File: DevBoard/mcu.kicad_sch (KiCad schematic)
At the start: 36 parts, among them J301 SWD, J302 UART debug, J303 Spare GPIO, U301 STM32WB1MMC

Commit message: Dev board: project footprints for holder, USB-C, half-bridge, module, EEPROM, BQ25756
- tools/make_footprints.py generates MonolithDev.pretty from the datasheets:
  BH-21700-B1BJ001 holder, Shou Han USB-C (with board-edge cutout),
  Infineon PG-TDSON-8-57 half-bridge (land + stencil), STM32WB1MMC LGA77,
  ST UFDFPN8 2x3 with the correct 1.2x1.4 exposed pad, and a 10 A net tie
- BQ25756 RRV0036A footprint from Antmicro (Apache-2.0), checked against TI
- Footprints assigned; R430/R530 become net-tie links, off the BOM and CPL
- Every symbol pin has a pad and vice versa; nets, ERC and overlaps unchanged

Co-Authored-By: Claude Opus 5.5 <noreply@anthropic.com>
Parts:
- U301: footprint (none) -> MonolithDev:ST_LGA-77_STM32WB1MMC_6.5x10mm
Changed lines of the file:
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@@
 		)
 		(property "Value" "0R"
-			(at 126.85 98.80 90)
+			(at 126.85 98.8 90)
 			(show_name no)
 			(do_not_autoplace no)
@@
 		(dnp no)
 		(property "Reference" "TH302"
-			(at 66.80 204.62 0)
+			(at 66.8 204.62 0)
 			(show_name no)
 			(do_not_autoplace no)
@@
 		)
 		(property "Value" "10k B3435"
-			(at 66.80 206.59 0)
+			(at 66.8 206.59 0)
 			(show_name no)
 			(do_not_autoplace no)
@@
 		(dnp no)
 		(property "Reference" "TH303"
-			(at 92.20 204.62 0)
+			(at 92.2 204.62 0)
 			(show_name no)
 			(do_not_autoplace no)
@@
 		)
 		(property "Value" "10k B3435"
-			(at 92.20 206.59 0)
+			(at 92.2 206.59 0)
 			(show_name no)
 			(do_not_autoplace no)
@@
 		(dnp no)
 		(property "Reference" "D301"
-			(at 71.43 237.80 0)
+			(at 71.43 237.8 0)
 			(show_name no)
 			(do_not_autoplace no)
@@
 		(dnp no)
 		(property "Reference" "TH304"
-			(at 117.60 204.62 0)
+			(at 117.6 204.62 0)
 			(show_name no)
 			(do_not_autoplace no)
@@
 		)
 		(property "Value" "10k B3435"
-			(at 117.60 206.59 0)
+			(at 117.6 206.59 0)
 			(show_name no)
 			(do_not_autoplace no)
@@
 		(dnp no)
 		(property "Reference" "U301"
-			(at 190.50 108.01 0)
+			(at 190.5 108.01 0)
 			(show_name no)
 			(do_not_autoplace no)
@@
 		)
 		(property "Value" "STM32WB1MMC"
-			(at 190.50 109.98 0)
+			(at 190.5 109.98 0)
 			(show_name no)
 			(do_not_autoplace no)
@@
 			)
 		)
-		(property "Footprint" ""
+		(property "Footprint" "MonolithDev:ST_LGA-77_STM32WB1MMC_6.5x10mm"
 			(at 190.5 139.7 0)
 			(hide yes)
@@
 		)
 		(property "Value" "GND"
-			(at 76.20 213.87 0)
+			(at 76.2 213.87 0)
 			(show_name no)
 			(do_not_autoplace no)
@@
 		(dnp no)
 		(property "Reference" "C311"
-			(at 139.87 200.80 0)
+			(at 139.87 200.8 0)
 			(show_name no)
 			(do_not_autoplace no)
@@
 		)
 		(property "Value" "GND"
-			(at 101.60 213.87 0)
+			(at 101.6 213.87 0)
 			(show_name no)
 			(do_not_autoplace no)
@@
 		)
 		(property "Value" "GND"
-			(at 161.22 127.00 90)
+			(at 161.22 127 90)
 			(show_name no)
 			(do_not_autoplace no)
@@
 		)
 		(property "Value" "GND"
-			(at 127.00 213.87 0)
+			(at 127 213.87 0)
 			(show_name no)
 			(do_not_autoplace no)
@@
 		(dnp no)
 		(property "Reference" "TH301"
-			(at 41.40 204.62 0)
+			(at 41.4 204.62 0)
 			(show_name no)
 			(do_not_autoplace no)
@@
 		)
 		(property "Value" "10k B3435"
-			(at 41.40 206.59 0)
+			(at 41.4 206.59 0)
 			(show_name no)
 			(do_not_autoplace no)
@@
 		)
 		(property "Value" "GND"
-			(at 50.80 213.87 0)
+			(at 50.8 213.87 0)
 			(show_name no)
 			(do_not_autoplace no)
@@
 		(dnp no)
 		(property "Reference" "J302"
-			(at 304.80 129.60 0)
+			(at 304.8 129.6 0)
 			(show_name no)
 			(do_not_autoplace no)
@@
 		)
 		(property "Value" "UART debug"
-			(at 304.80 131.57 0)
+			(at 304.8 131.57 0)
 			(show_name no)
 			(do_not_autoplace no)
@@
 		)
 		(property "Value" "GND"
-			(at 139.70 113.54 0)
+			(at 139.7 113.54 0)
 			(show_name no)
 			(do_not_autoplace no)
@@
 		(dnp no)
 		(property "Reference" "J303"
-			(at 312.90 164.12 0)
+			(at 312.9 164.12 0)
 			(show_name no)
 			(do_not_autoplace no)
@@
 		)
 		(property "Value" "Spare GPIO"
-			(at 312.90 166.08 0)
+			(at 312.9 166.08 0)
 			(show_name no)
 			(do_not_autoplace no)
@@
 		(dnp no)
 		(property "Reference" "TP305"
-			(at 292.10 258.31 0)
+			(at 292.1 258.31 0)
 			(show_name no)
 			(do_not_autoplace no)
@@
 		)
 		(property "Value" "GND"
-			(at 93.98 250.70 0)
+			(at 93.98 250.7 0)
 			(show_name no)
 			(do_not_autoplace no)

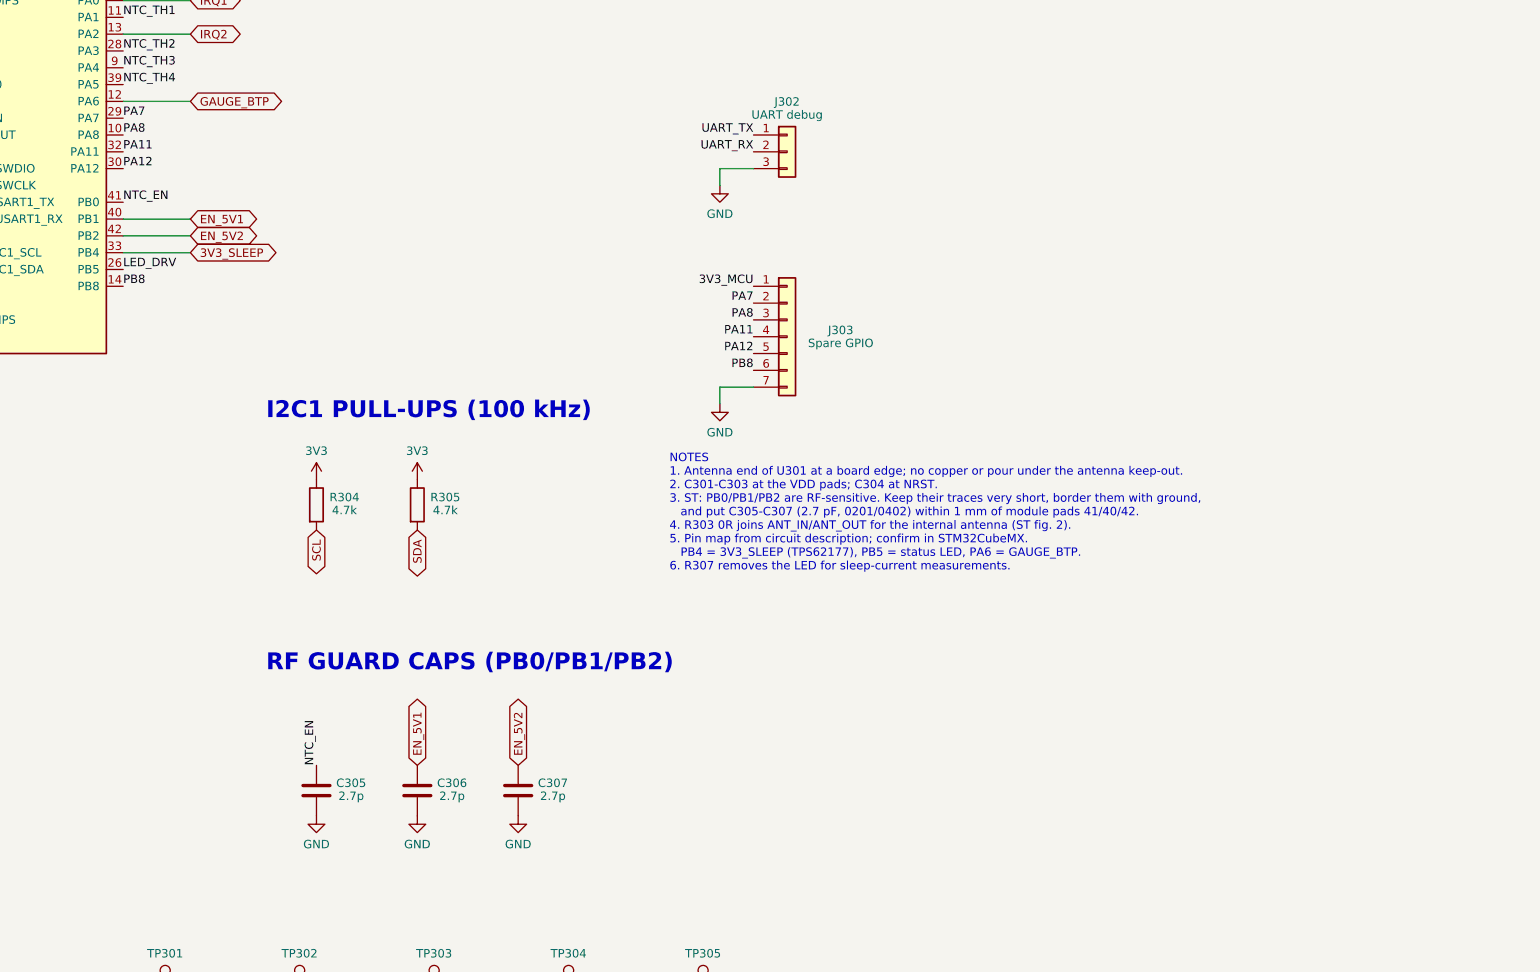
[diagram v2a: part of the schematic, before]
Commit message: Dev board design review: free PB0-PB2, document PB4 reset state
- NTC_EN, EN_5V1, EN_5V2 move from PB0/PB1/PB2 (ST: RF-sensitive, leave
  unconnected) to PA8/PA11/PA12; C305-C307 guard caps removed, no-connects added;
  J303 now brings out PA7, PB8 and the three enables
- Pin map checked against DS13258 table 15 (ADC, wake-up, I2C1, USART1, SWD)
- PB4 resets as NJTRST with pull-up, so the TPS62177 boots in normal mode,
  not sleep mode as documented; notes and docs corrected
- MCU notes: module placement per ST's reference PCB

Co-Authored-By: Claude Opus 5.5 <noreply@anthropic.com>
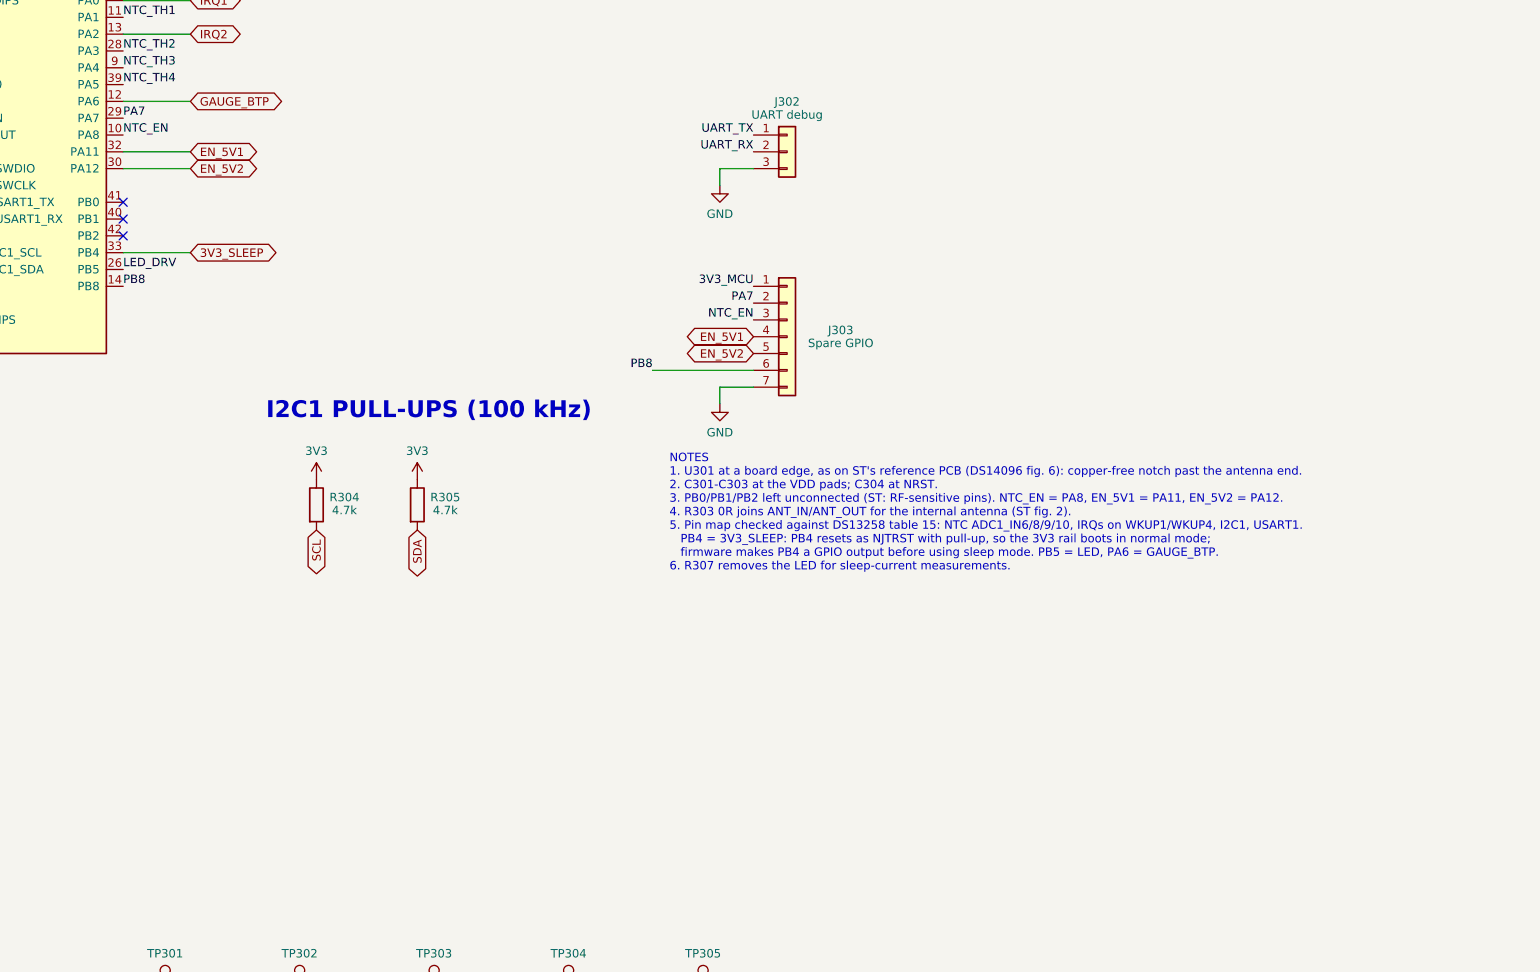
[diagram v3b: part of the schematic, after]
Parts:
- removed C305, C306, C307: 2.7p, Capacitor_SMD:C_0402_1005Metric, symbol Device:C
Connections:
- net PA11 is gone; now on net EN_5V1: J303.4 (Pin_4), U301.32 (PA11)
- net PA12 is gone; now on net EN_5V2: J303.5 (Pin_5), U301.30 (PA12)
- net PA8 is gone; now on net NTC_EN: J303.3 (Pin_3), U301.10 (PA8)
- net EN_5V1: no longer U301.40 (PB1)
- net EN_5V2: no longer U301.42 (PB2)
- net NTC_EN: no longer U301.41 (PB0)
- no-connect marks 3 -> 6
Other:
- note added: "NOTES 1. U301 at a board edge, as on ST's reference PCB (DS14096 fig. 6): copper-free notch past the antenna end. 2. C301-C303 at the VDD pads; C304 at NRST. 3. PB0/PB1/PB2 left unconnected (ST: RF-sensitive pins). NTC_EN = PA8, EN_5V1 = PA11, EN_5V2 = PA12. 4. R303 0R joins ANT_IN/ANT_OUT for the internal antenna (ST fig. 2). 5. Pin map checked against DS13258 table 15: NTC ADC1_IN6/8/9/10, IRQs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"
- note removed: "NOTES 1. Antenna end of U301 at a board edge; no copper or pour under the antenna keep-out. 2. C301-C303 at the VDD pads; C304 at NRST. 3. ST: PB0/PB1/PB2 are RF-sensitive. Keep their traces very short, border them with ground, and put C305-C307 (2.7 pF, 0201/0402) within 1 mm of module pads 41/40/42. 4. R303 0R joins ANT_IN/ANT_OUT for the internal antenna (ST fig. 2). 5. Pin map from circuit de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"
- note removed: "RF GUARD CAPS (PB0/PB1/PB2)"

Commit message: Dev board rev A4: design-review fixes, polymer bulk, charge inhibit
Schematic design review (three reviewers, cross-challenged) in
docs/devboard/schematic-review-2026-10-12.md, and its fixes:
- U203 TPS70950 EN no longer tied to PACK_P (would destroy it)
- ICHG 17.8k: 2.8 A per port (was 9.8 A, above the cells' 5.6 A)
- U101 footprint from TI RSM0032A (1.4 mm thermal pad, was 2.8 mm)
- D+/D- ESD now 5 V PESD5V0S2BT (TPS25751 GPIO4/5 are rated 6 V)
- R101-R104 1206, F101 and J101 DNP, DNP gate parts on Q102
- BTP_INT buffered by a 2N7002; SMBus pull-ups on a removable 0R
- Wake button, bench PACK_P header, reset, BOOT0/3V3_SLEEP pads,
  J303 series resistors, IRQ pull-ups, vertical SMAs, BOM ratings

Open-question decisions: CHG_INH (PB8 -> each BQ25756 CE) lets the
MCU stop charging independently of the TPS25751; J103 in EV2400
SMBus pin order; "fit cells before USB" silkscreen.

Charger bulk banks now one solid polymer cap plus the MLCCs at the
FETs (16 fewer MLCCs). PWR_FLAGs moved to where each rail is sourced.
Board: footprints swapped/added and placed, DRC clean before routing.

Co-Authored-By: Claude Opus 5.5 <noreply@anthropic.com>
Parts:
- added R312: 0R, Resistor_SMD:R_0603_1608Metric, symbol Device:R
- added R313, R314, R315: 100k, Resistor_SMD:R_0603_1608Metric, symbol Device:R
- added R316, R317, R318, R319: 1k, Resistor_SMD:R_0603_1608Metric, symbol Device:R
- added SW301: RESET, Button_Switch_SMD:SW_Push_1P1T_XKB_TS-1187A, symbol Switch:SW_Push
- added TP306: BOOT0, TestPoint:TestPoint_Pad_D1.5mm, symbol Connector:TestPoint
- added TP307: 3V3_SLEEP, TestPoint:TestPoint_Pad_D1.5mm, symbol Connector:TestPoint
- added TP308: SMB_PU, TestPoint:TestPoint_Keystone_5000-5004_Miniature, symbol Connector:TestPoint
- C301: value 4.7u -> 4.7u 16V; LCSC (none) -> C19666; MPN (none) -> CL10A475KO8NNNC
- C302, C303, C304: value 0.1u -> 0.1u 50V; LCSC (none) -> C307331; MPN (none) -> CL05B104KB54PNC
- C308, C309, C310, C311: value 0.1u -> 0.1u 50V; LCSC (none) -> C14663; MPN (none) -> CC0603KRX7R9BB104
- D301: LCSC (none) -> C72043; MPN (none) -> 19-217/GHC-YR1S2/3T
- J301: footprint Connector_PinHeader_1.27mm:PinHeader_2x05_P1.27mm_Vertical -> Connector_PinHeader_1.27mm:PinHeader_2x05_P1.27mm_Vertical_SMD; MPN (none) -> Samtec FTSH-105-01-L-DV-K; Notes Cortex 10-pin -> Keyed (pin 7 removed) so standard Cortex debug cables only 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
- TH301, TH302, TH303, TH304: LCSC (none) -> C13564; MPN (none) -> NCP18XH103F03RB
- U301: LCSC (none) -> C5456183; MPN (none) -> STM32WB1MMCH6TR; Notes (none) -> LGA-77, JLC-placed only: check JLC stock at order time (LCS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
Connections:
- net 3V3: now also R312.1, R313.1, R314.1, R315.1; no longer R304.1, R305.1
- net 3V3_SLEEP: now also R313.2, TP307.1
- net EN_5V1: now also R317.1; no longer J303.4 (Pin_4)
- net EN_5V2: now also R318.1; no longer J303.5 (Pin_5)
- net GND: now also SW301.2
- net IRQ1: now also R314.2
- net IRQ2: now also R315.2
- net NRST: now also SW301.1
- net NTC_EN: now also R316.1; no longer J303.3 (Pin_3)
- net at R302.1, U301.22 (BOOT0): now also TP306.1
- net PB8 renamed CHG_INH
- net CHG_INH: now also R319.1; no longer J303.6 (Pin_6)
- new net J303_CHG_INH: J303.6 (Pin_6), R319.2
- new net J303_EN_5V1: J303.4 (Pin_4), R317.2
- new net J303_EN_5V2: J303.5 (Pin_5), R318.2
- new net J303_NTC_EN: J303.3 (Pin_3), R316.2
- new net SMB_PU: R304.1, R305.1, R312.2, TP308.1
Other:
- note added: "BRING-UP AIDS"
- note added: "I2C1 + IRQ PULL-UPS"
- note removed: "I2C1 PULL-UPS (100 kHz)"

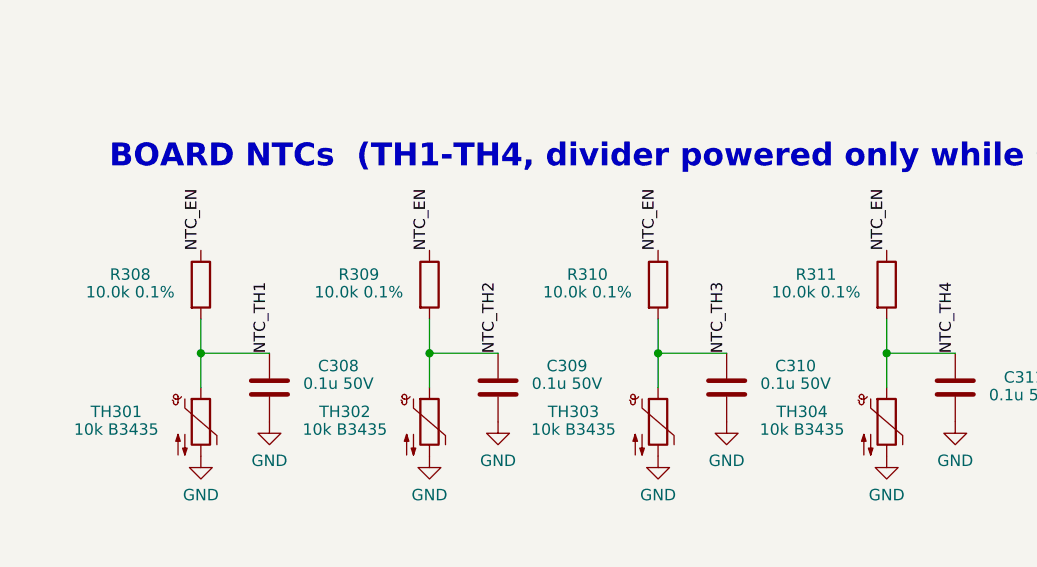
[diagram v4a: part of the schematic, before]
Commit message: Dev board: bootstrap diodes, one NTC per cell, 1 % resistors
- BQ25756 bootstrap Schottkys DRV_SUP -> BTST1/BTST2 on both ports
  (TI BQ25756 schematic checklist D2/D3, required; LRB521S-40T1G,
  SOD-523), placed in line with the BTST caps. Also added to the
  production BOM/netlist.
- Gauge TS2-TS4 no longer tied to VSS: J105-J107 take a wired 10k NTC
  per cell; all four NTC headers sit beside their cell's tap test point.
- Precision resistors rounded to stocked UNI-ROYAL 1 % parts (ICHG
  9.1k, ILIM 3.6k, TS 1.8k/5.6k, FSW/ACUV-ACOV, NTC dividers); only the
  charge-voltage and PP5V feedback dividers stay 0.1 %.

Co-Authored-By: Claude Opus 5.5 <noreply@anthropic.com>
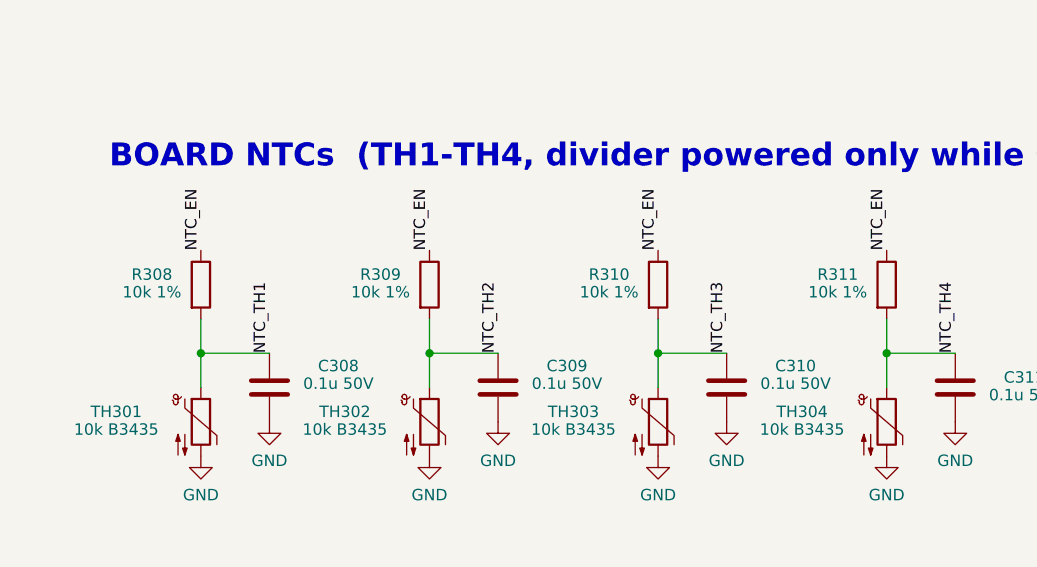
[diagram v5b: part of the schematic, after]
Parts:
- R308, R309, R310, R311: value 10.0k 0.1% -> 10k 1%; LCSC C110775 -> C17414; MPN RT0805BRD0710KL -> 0805W8F1002T5E; Notes (none) -> NTC divider: 1 % costs about 0.25 C at 25 C (the NTC itself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
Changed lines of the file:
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@@
 		(dnp no)
 		(property "Reference" "R310"
-			(at 93.75 189.37 0)
-			(show_name no)
-			(do_not_autoplace no)
-			(effects
-				(font
-					(size 1.27 1.27)
-				)
-			)
-		)
-		(property "Value" "10.0k 0.1%"
-			(at 93.75 191.33 0)
+			(at 96.16 189.37 0)
+			(show_name no)
+			(do_not_autoplace no)
+			(effects
+				(font
+					(size 1.27 1.27)
+				)
+			)
+		)
+		(property "Value" "10k 1%"
+			(at 96.16 191.33 0)
 			(show_name no)
 			(do_not_autoplace no)
@@
 			)
 		)
-		(property "LCSC" "C110775"
+		(property "LCSC" "C17414"
 			(at 101.6 190.5 0)
 			(hide yes)
@@
 			)
 		)
-		(property "MPN" "RT0805BRD0710KL"
+		(property "MPN" "0805W8F1002T5E"
+			(at 101.6 190.5 0)
+			(hide yes)
+			(show_name no)
+			(do_not_autoplace no)
+			(effects
+				(font
+					(size 1.27 1.27)
+				)
+			)
+		)
+		(property "Notes" "NTC divider: 1 % costs about 0.25 C at 25 C (the NTC itself is 1 %)"
 			(at 101.6 190.5 0)
 			(hide yes)
@@
 		(dnp no)
 		(property "Reference" "R309"
-			(at 68.35 189.37 0)
-			(show_name no)
-			(do_not_autoplace no)
-			(effects
-				(font
-					(size 1.27 1.27)
-				)
-			)
-		)
-		(property "Value" "10.0k 0.1%"
-			(at 68.35 191.33 0)
+			(at 70.76 189.37 0)
+			(show_name no)
+			(do_not_autoplace no)
+			(effects
+				(font
+					(size 1.27 1.27)
+				)
+			)
+		)
+		(property "Value" "10k 1%"
+			(at 70.76 191.33 0)
 			(show_name no)
 			(do_not_autoplace no)
@@
 			)
 		)
-		(property "LCSC" "C110775"
+		(property "LCSC" "C17414"
 			(at 76.2 190.5 0)
 			(hide yes)
@@
 			)
 		)
-		(property "MPN" "RT0805BRD0710KL"
+		(property "MPN" "0805W8F1002T5E"
+			(at 76.2 190.5 0)
+			(hide yes)
+			(show_name no)
+			(do_not_autoplace no)
+			(effects
+				(font
+					(size 1.27 1.27)
+				)
+			)
+		)
+		(property "Notes" "NTC divider: 1 % costs about 0.25 C at 25 C (the NTC itself is 1 %)"
 			(at 76.2 190.5 0)
 			(hide yes)
@@
 		(dnp no)
 		(property "Reference" "R311"
-			(at 119.15 189.37 0)
-			(show_name no)
-			(do_not_autoplace no)
-			(effects
-				(font
-					(size 1.27 1.27)
-				)
-			)
-		)
-		(property "Value" "10.0k 0.1%"
-			(at 119.15 191.33 0)
+			(at 121.56 189.37 0)
+			(show_name no)
+			(do_not_autoplace no)
+			(effects
+				(font
+					(size 1.27 1.27)
+				)
+			)
+		)
+		(property "Value" "10k 1%"
+			(at 121.56 191.33 0)
 			(show_name no)
 			(do_not_autoplace no)
@@
 			)
 		)
-		(property "LCSC" "C110775"
+		(property "LCSC" "C17414"
 			(at 127 190.5 0)
 			(hide yes)
@@
 			)
 		)
-		(property "MPN" "RT0805BRD0710KL"
+		(property "MPN" "0805W8F1002T5E"
+			(at 127 190.5 0)
+			(hide yes)
+			(show_name no)
+			(do_not_autoplace no)
+			(effects
+				(font
+					(size 1.27 1.27)
+				)
+			)
+		)
+		(property "Notes" "NTC divider: 1 % costs about 0.25 C at 25 C (the NTC itself is 1 %)"
 			(at 127 190.5 0)
 			(hide yes)
@@
 		(dnp no)
 		(property "Reference" "R308"
-			(at 42.95 189.37 0)
-			(show_name no)
-			(do_not_autoplace no)
-			(effects
-				(font
-					(size 1.27 1.27)
-				)
-			)
-		)
-		(property "Value" "10.0k 0.1%"
-			(at 42.95 191.33 0)
+			(at 45.36 189.37 0)
+			(show_name no)
+			(do_not_autoplace no)
+			(effects
+				(font
+					(size 1.27 1.27)
+				)
+			)
+		)
+		(property "Value" "10k 1%"
+			(at 45.36 191.33 0)
 			(show_name no)
 			(do_not_autoplace no)
@@
 			)
 		)
-		(property "LCSC" "C110775"
+		(property "LCSC" "C17414"
 			(at 50.8 190.5 0)
 			(hide yes)
@@
 			)
 		)
-		(property "MPN" "RT0805BRD0710KL"
+		(property "MPN" "0805W8F1002T5E"
 			(at 50.8 190.5 0)
 			(hide yes)
+			(show_name no)
+			(do_not_autoplace no)
+			(effects
+				(font
+					(size 1.27 1.27)
+				)
+			)
+		)
+		(property "Notes" "NTC divider: 1 % costs about 0.25 C at 25 C (the NTC itself is 1 %)"
+			(at 50.8 190.5 0)
+			(hide yes)
